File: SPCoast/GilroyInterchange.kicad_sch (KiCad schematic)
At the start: 71 parts, among them SW5777 777, SW5781 781

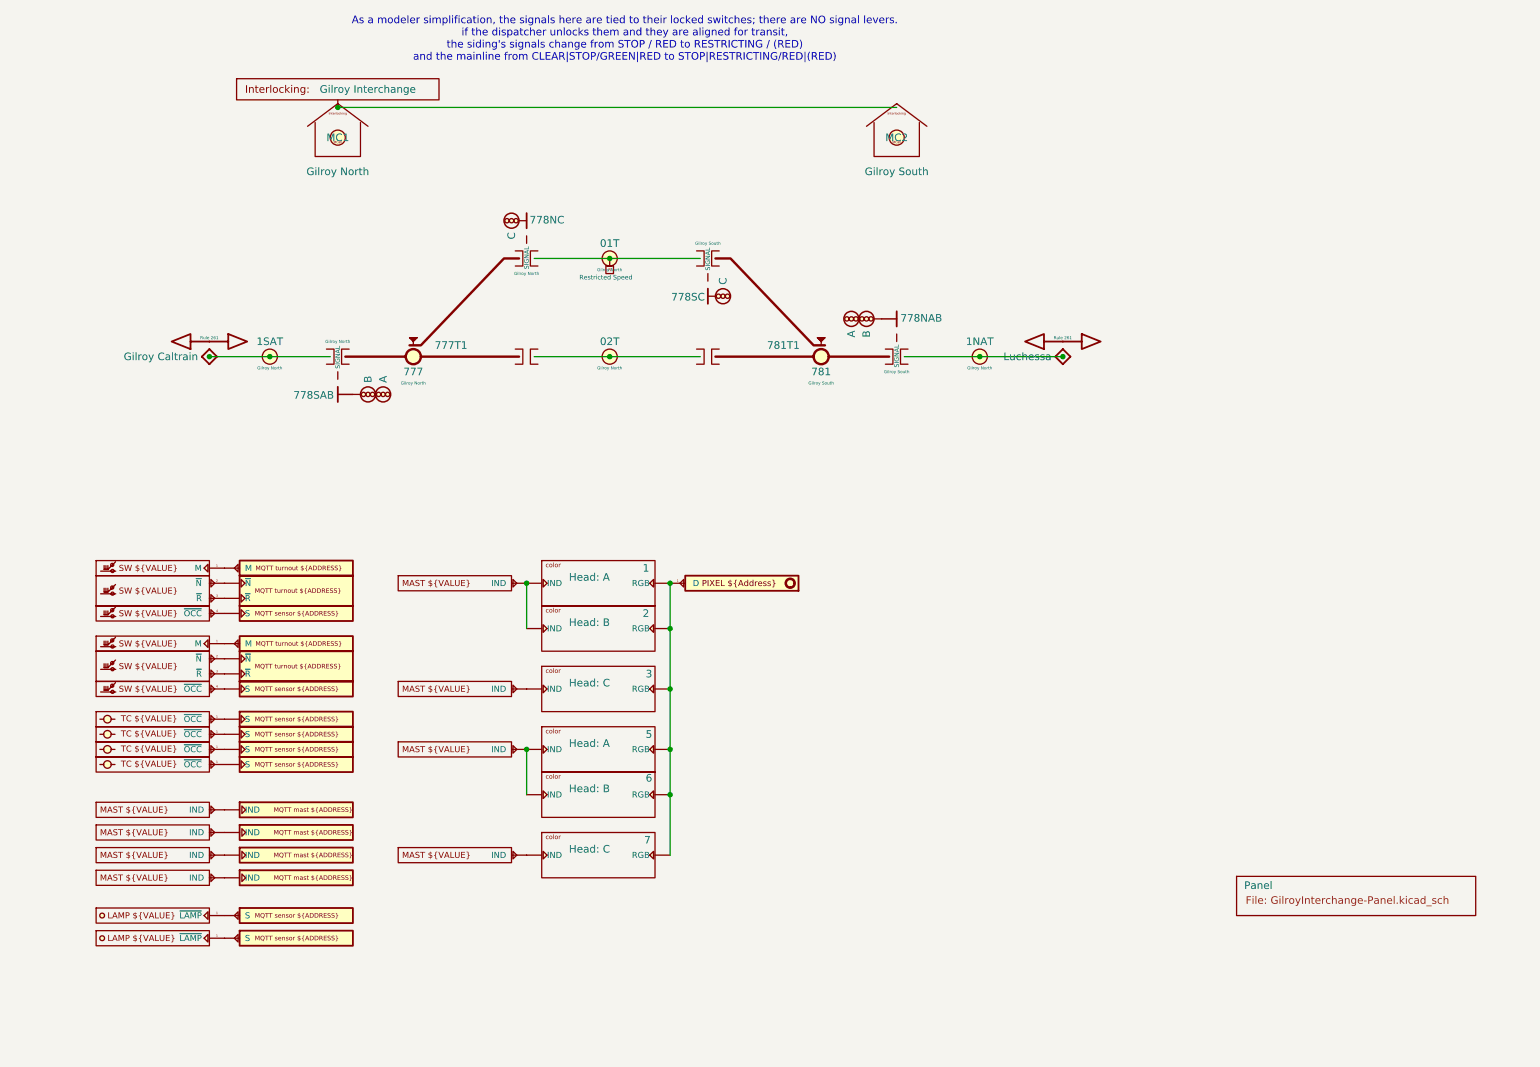
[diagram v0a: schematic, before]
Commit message: chore(kicad): owner mockup: explicit seam wiring on Luchessa and South-cTc, host and bus pins
Owner's edits, committed as they stand (2026-10-21), before scripted edits build on them.

- Interlocking gains Codeline and Host pins; MAIN HOUSE's Interlocking pin is Codeline.
- OfficeUnit gains Host and Codeline pins; JohnCTC desk processor drawn on South-cTc.
- Processor gains Transport and IO pins; MAX7313 and MCP23017 gain an I2C bus pin.
- Transports: Codeline pin renamed Host; JMRI_MQTT instance added; Loconet removed.
- Encodings' pin renamed Transport; Luchessa's 506 and Bit Packing instances removed.
- SPCoastApp virtual host (FieldUnit_Virtual) hosts CMRInet and JMRI_MQTT.
- Luchessa: unit, houses and Time Coded on one net; Host to its own processor;
  panel MAX7313s on the desk bus (OfficeBus).
- Watsonville, Caltrain, Interchange: first-pass Processor placeholders, to be redrawn.

Verified: netlist and ERC exported from the saved project; field diff against the
committed netlist shows no per-instance field lost.
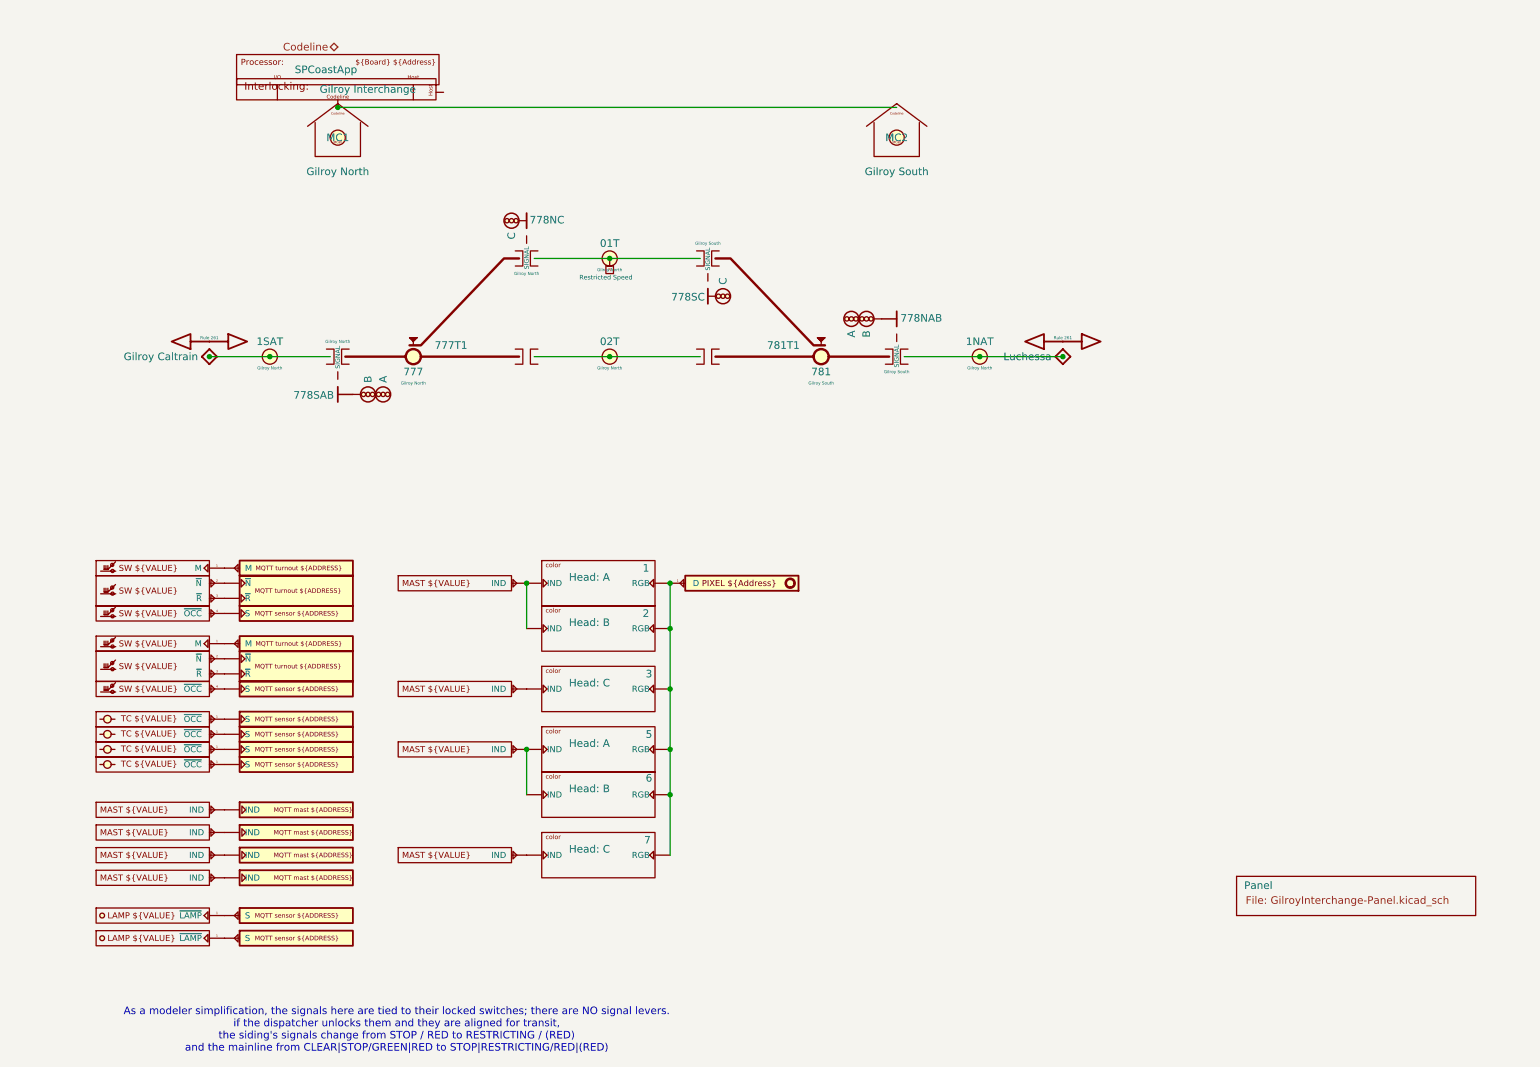
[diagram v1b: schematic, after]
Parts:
- added Proc2: SPCoastApp, symbol Railroad-HardwareIO:Processor
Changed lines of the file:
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@@
 	(text "As a modeler simplification, the signals here are tied to their locked switches; there are NO signal levers.\nif the dispatcher unlocks them and they are aligned for transit, \nthe siding's signals change from STOP / RED to RESTRICTING / (RED)\nand the mainline from CLEAR|STOP/GREEN|RED to STOP|RESTRICTING/RED|(RED)"
 		(exclude_from_sim no)
-		(at 123.19 24.13 0)
+		(at 84.836 190.754 0)
 		(effects
 			(font
@@
 		)
 	)
+	(hierarchical_label "Codeline"
+		(shape bidirectional)
+		(at 74.93 25.4 180)
+		(effects
+			(font
+				(size 1.27 1.27)
+			)
+			(justify right)
+		)
+	)
 	(symbol
 		(lib_id "Railroad-Trackplan:IRJ-Signal")
@@
 	)
 	(symbol
+		(lib_id "Railroad-HardwareIO:Processor")
+		(at 74.93 29.21 0)
+		(unit 1)
+		(body_style 1)
+		(exclude_from_sim no)
+		(in_bom yes)
+		(on_board yes)
+		(in_pos_files yes)
+		(dnp no)
+		(fields_autoplaced yes)
+		(property "Reference" "Proc2"
+			(at 60.706 23.368 0)
+			(hide yes)
+			(show_name no)
+			(do_not_autoplace yes)
+			(effects
+				(font
+					(size 1.27 1.27)
+				)
+			)
+		)
+		(property "Value" "SPCoastApp"
+			(at 67.691 29.21 0)
+			(show_name no)
+			(do_not_autoplace yes)
+			(effects
+				(font
+					(size 1.27 1.27)
+				)
+				(justify left)
+			)
+		)
+		(property "Footprint" ""
+			(at 74.93 29.21 0)
+			(hide yes)
+			(show_name no)
+			(do_not_autoplace no)
+			(effects
+				(font
+					(size 1.27 1.27)
+				)
+			)
+		)
+		(property "Datasheet" ""
+			(at 74.93 29.21 0)
+			(hide yes)
+			(show_name no)
+			(do_not_autoplace no)
+			(effects
+				(font
+					(size 1.27 1.27)
+				)
+			)
+		)
+		(property "Description" "A processor: declares the I2C bus and GPIO pins of the chips and drivers in its scope; with Transport and Address it is a node on that code line."
+			(at 76.2 33.02 0)
+			(hide yes)
+			(show_name no)
+			(do_not_autoplace no)
+			(effects
+				(font
+					(size 1.27 1.27)
+				)
+			)
+		)
+		(property "Role" "STRUCTURE"
+			(at 63.627 19.558 0)
+			(hide yes)
+			(show_name no)
+			(do_not_autoplace no)
+			(effects
+				(font
+					(size 1.27 1.27)
+				)
+			)
+		)
+		(property "Kind" "PROCESSOR"
+			(at 65.024 21.209 0)
+			(hide yes)
+			(show_name no)
+			(do_not_autoplace no)
+			(effects
+				(font
+					(size 1.27 1.27)
+				)
+			)
+		)
+		(property "Board" ""
+			(at 74.93 29.21 0)
+			(hide yes)
+			(show_name no)
+			(do_not_autoplace no)
+			(effects
+				(font
+					(size 1.27 1.27)
+				)
+			)
+		)
+		(property "Transport" ""
+			(at 74.93 29.21 0)
+			(hide yes)
+			(show_name no)
+			(do_not_autoplace no)
+			(effects
+				(font
+					(size 1.27 1.27)
+				)
+			)
+		)
+		(property "Address" "WhatGoesHere"
+			(at 74.93 29.21 0)
+			(hide yes)
+			(show_name no)
+			(do_not_autoplace no)
+			(effects
+				(font
+					(size 1.27 1.27)
+				)
+			)
+		)
+		(pin "1"
+		)
+		(pin "2"
+		)
+		(instances
+			(project "SPCoast"
+				(path "/528348b2-add8-5367-a5f7-439c76f0ca33/2ed995e3-3819-55cd-b8d9-5c2af048ccb4/defc570c-1f61-4751-be37-2827b304f837"
+					(reference "Proc2")
+					(unit 1)
+				)
+			)
+		)
+	)
+	(symbol
 		(lib_id "Railroad-HardwareIO:Driver-JMRI-Turnout")
 		(at 55.88 113.03 0)
@@
 		(pin "1"
 		)
+		(pin "2"
+		)
 		(instances
